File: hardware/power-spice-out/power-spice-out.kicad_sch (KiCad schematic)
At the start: 10 parts, among them Q1 Si7149ADP, Q2 NMOS, Q3 Si7149ADP

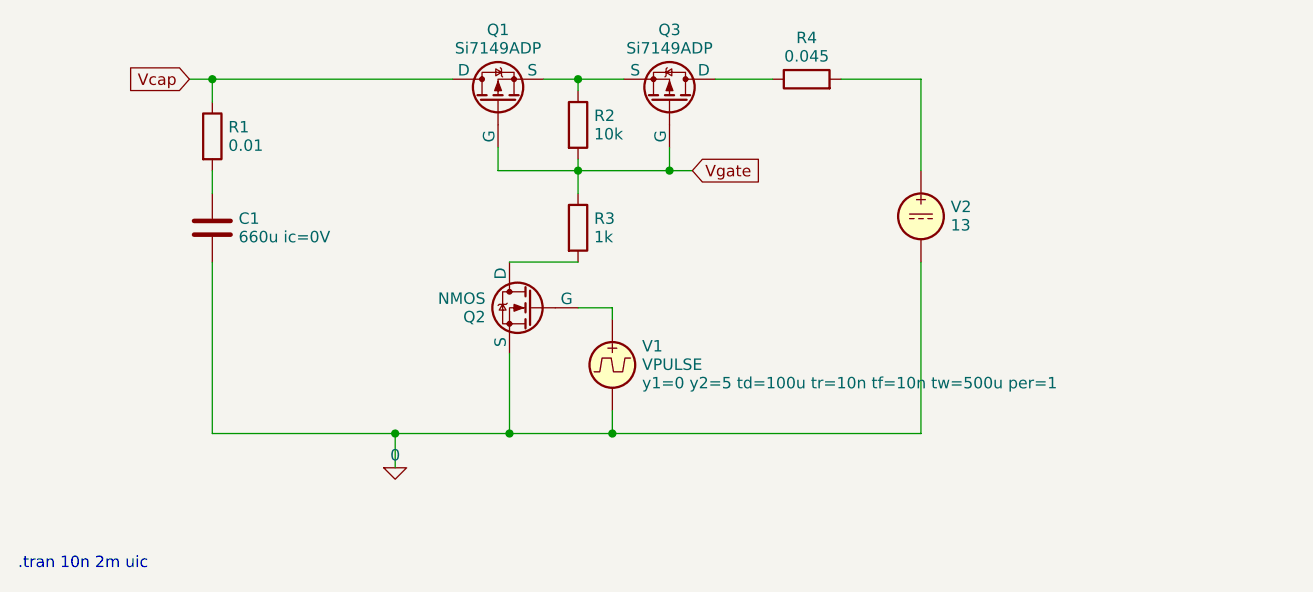
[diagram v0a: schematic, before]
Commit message: More accurate simulation with a BSS123 model and the 10k resistance from the control circuit. Doesn't change the peak transient current ...
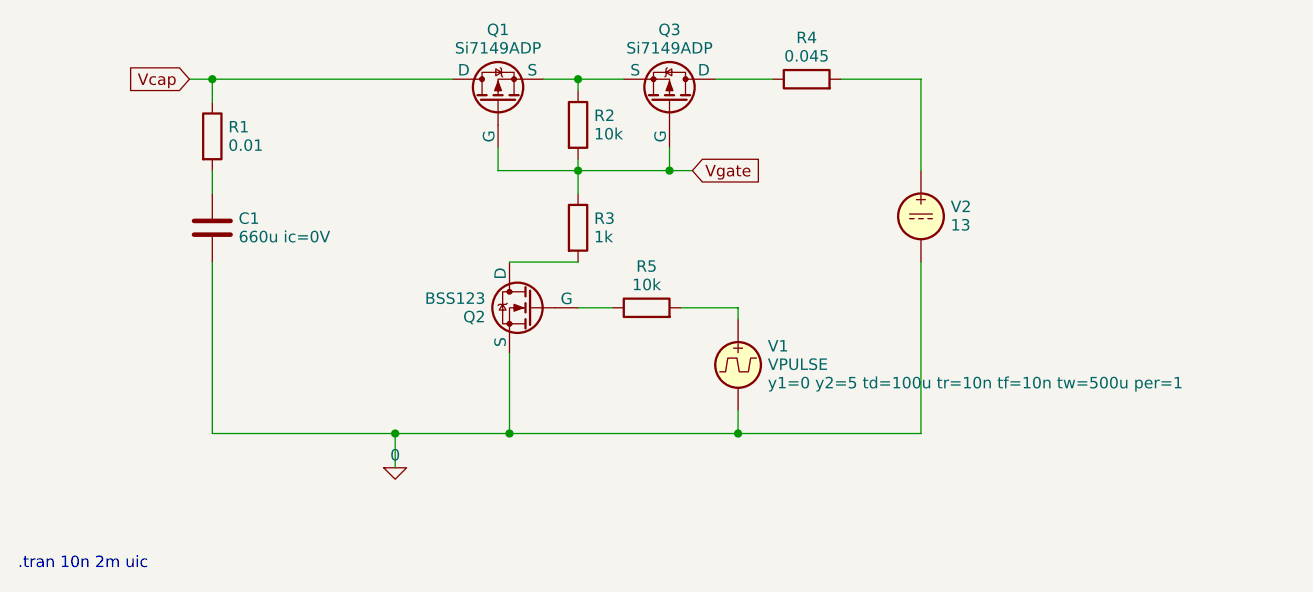
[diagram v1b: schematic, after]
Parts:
- added R5: 10k, symbol Device:R
- Q2: value NMOS -> BSS123
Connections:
- net at Q2.2 (G): now also R5.1; no longer V1.1
- new net: R5.2, V1.1
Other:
- moved on the sheet: V1
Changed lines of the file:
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@@
   (junction (at 116.84 91.44) (diameter 0) (color 0 0 0 0)
   )
-  (junction (at 161.29 130.81) (diameter 0) (color 0 0 0 0)
-  )
   (junction (at 149.86 130.81) (diameter 0) (color 0 0 0 0)
   )
   (junction (at 157.48 101.6) (diameter 0) (color 0 0 0 0)
   )
+  (junction (at 175.26 130.81) (diameter 0) (color 0 0 0 0)
+  )
   (junction (at 137.16 130.81) (diameter 0) (color 0 0 0 0)
   )
@@
     (stroke (width 0) (type default))
   )
-  (wire (pts (xy 161.29 130.81) (xy 149.86 130.81))
-    (stroke (width 0) (type default))
-  )
   (wire (pts (xy 172.72 91.44) (xy 179.07 91.44))
     (stroke (width 0) (type default))
@@
     (stroke (width 0) (type default))
   )
+  (wire (pts (xy 168.91 116.84) (xy 175.26 116.84))
+    (stroke (width 0) (type default))
+  )
+  (wire (pts (xy 149.86 130.81) (xy 175.26 130.81))
+    (stroke (width 0) (type default))
+  )
   (wire (pts (xy 149.86 130.81) (xy 137.16 130.81))
     (stroke (width 0) (type default))
@@
     (stroke (width 0) (type default))
   )
-  (wire (pts (xy 195.58 130.81) (xy 161.29 130.81))
+  (wire (pts (xy 195.58 130.81) (xy 175.26 130.81))
     (stroke (width 0) (type default))
   )
@@
     (stroke (width 0) (type default))
   )
-  (wire (pts (xy 161.29 128.27) (xy 161.29 130.81))
+  (wire (pts (xy 175.26 128.27) (xy 175.26 130.81))
     (stroke (width 0) (type default))
   )
@@
     (stroke (width 0) (type default))
   )
-  (wire (pts (xy 161.29 116.84) (xy 161.29 118.11))
+  (wire (pts (xy 175.26 116.84) (xy 175.26 118.11))
     (stroke (width 0) (type default))
   )
@@
     )
   )
+  (symbol (lib_id "Device:R") (at 165.1 116.84 90) (unit 1)
+    (in_bom yes) (on_board yes) (dnp no) (fields_autoplaced)
+    (property "Reference" "R5" (at 165.1 112.244 90)
+      (effects (font (size 1.27 1.27)))
+    )
+    (property "Value" "10k" (at 165.1 114.292 90)
+      (effects (font (size 1.27 1.27)))
+    )
+    (property "Footprint" "" (at 165.1 118.618 90)
+      (effects (font (size 1.27 1.27)) hide)
+    )
+    (property "Datasheet" "~" (at 165.1 116.84 0)
+      (effects (font (size 1.27 1.27)) hide)
+    )
+    (property "P/N" "" (at 165.1 116.84 0)
+      (effects (font (size 1.27 1.27)) hide)
+    )
+    (pin "1")
+    (pin "2")
+    (instances
+      (project "power-spice-out"
+        (path "/3b519c6d-240e-4784-9341-b4b14767d2f5"
+          (reference "R5") (unit 1)
+        )
+      )
+    )
+  )
   (symbol (lib_id "Simulation_SPICE:NMOS") (at 152.4 116.84 0) (mirror y) (unit 1)
     (in_bom yes) (on_board yes) (dnp no)
@@
       (effects (font (size 1.27 1.27)) (justify left))
     )
-    (property "Value" "NMOS" (at 147.1931 115.816 0)
+    (property "Value" "BSS123" (at 147.1931 115.816 0)
       (effects (font (size 1.27 1.27)) (justify left))
     )
@@
       (effects (font (size 1.27 1.27)) hide)
     )
-    (property "Sim.Device" "NMOS" (at 152.4 133.985 0)
-      (effects (font (size 1.27 1.27)) hide)
-    )
-    (property "Sim.Type" "VDMOS" (at 152.4 135.89 0)
-      (effects (font (size 1.27 1.27)) hide)
-    )
-    (property "Sim.Pins" "1=D 2=G 3=S" (at 152.4 132.08 0)
+    (property "Sim.Device" "SUBCKT" (at 152.4 133.985 0)
+      (effects (font (size 1.27 1.27)) hide)
+    )
+    (property "Sim.Pins" "1=3 2=4 3=5" (at 152.4 132.08 0)
       (effects (font (size 1.27 1.27)) hide)
     )
@@
       (effects (font (size 1.27 1.27)) hide)
     )
+    (property "Sim.Library" "BSS123.LIB" (at 152.4 116.84 0)
+      (effects (font (size 1.27 1.27)) hide)
+    )
+    (property "Sim.Name" "BSS123/ZTX" (at 152.4 116.84 0)
+      (effects (font (size 1.27 1.27)) hide)
+    )
     (pin "1")
     (pin "2")
@@
     )
   )
-  (symbol (lib_id "Simulation_SPICE:VPULSE") (at 161.29 123.19 0) (unit 1)
-    (in_bom yes) (on_board yes) (dnp no) (fields_autoplaced)
-    (property "Reference" "V1" (at 164.592 121.1062 0)
-      (effects (font (size 1.27 1.27)) (justify left))
-    )
-    (property "Value" "VPULSE" (at 164.592 123.1542 0)
-      (effects (font (size 1.27 1.27)) (justify left))
-    )
-    (property "Footprint" "" (at 161.29 123.19 0)
-      (effects (font (size 1.27 1.27)) hide)
-    )
-    (property "Datasheet" "~" (at 161.29 123.19 0)
-      (effects (font (size 1.27 1.27)) hide)
-    )
-    (property "Sim.Pins" "1=+ 2=-" (at 161.29 123.19 0)
-      (effects (font (size 1.27 1.27)) hide)
-    )
-    (property "Sim.Type" "PULSE" (at 161.29 123.19 0)
-      (effects (font (size 1.27 1.27)) hide)
-    )
-    (property "Sim.Device" "V" (at 161.29 123.19 0)
+  (symbol (lib_id "Simulation_SPICE:VPULSE") (at 175.26 123.19 0) (unit 1)
+    (in_bom yes) (on_board yes) (dnp no) (fields_autoplaced)
+    (property "Reference" "V1" (at 178.562 121.1062 0)
+      (effects (font (size 1.27 1.27)) (justify left))
+    )
+    (property "Value" "VPULSE" (at 178.562 123.1542 0)
+      (effects (font (size 1.27 1.27)) (justify left))
+    )
+    (property "Footprint" "" (at 175.26 123.19 0)
+      (effects (font (size 1.27 1.27)) hide)
+    )
+    (property "Datasheet" "~" (at 175.26 123.19 0)
+      (effects (font (size 1.27 1.27)) hide)
+    )
+    (property "Sim.Pins" "1=+ 2=-" (at 175.26 123.19 0)
+      (effects (font (size 1.27 1.27)) hide)
+    )
+    (property "Sim.Type" "PULSE" (at 175.26 123.19 0)
+      (effects (font (size 1.27 1.27)) hide)
+    )
+    (property "Sim.Device" "V" (at 175.26 123.19 0)
       (effects (font (size 1.27 1.27)) (justify left) hide)
     )
-    (property "Sim.Params" "y1=0 y2=5 td=100u tr=10n tf=10n tw=500u per=1" (at 164.592 125.2022 0)
-      (effects (font (size 1.27 1.27)) (justify left))
-    )
+    (property "Sim.Params" "y1=0 y2=5 td=100u tr=10n tf=10n tw=500u per=1" (at 178.562 125.2022 0)
+      (effects (font (size 1.27 1.27)) (justify left))
+    )

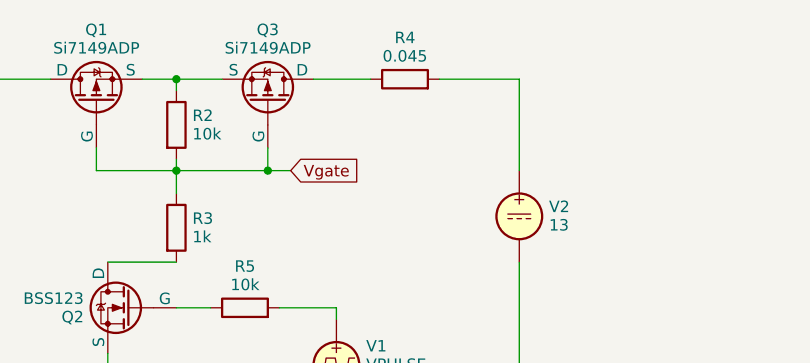
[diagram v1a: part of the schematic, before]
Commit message: Correct "shunt+cables" resistor value (shunt is 2mO, not 20mO)
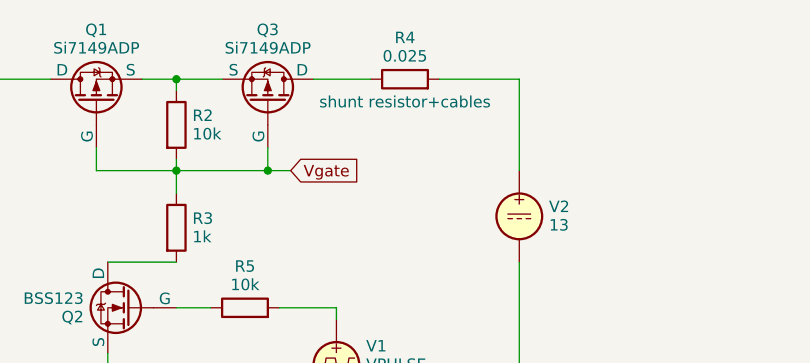
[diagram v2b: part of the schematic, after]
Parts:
- R4: value 0.045 -> 0.025; comment (none) -> shunt resistor+cables
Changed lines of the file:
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@@
   )
   (symbol (lib_id "Device:R") (at 182.88 91.44 90) (unit 1)
-    (in_bom yes) (on_board yes) (dnp no) (fields_autoplaced)
+    (in_bom yes) (on_board yes) (dnp no)
     (property "Reference" "R4" (at 182.88 86.844 90)
       (effects (font (size 1.27 1.27)))
     )
-    (property "Value" "0.045" (at 182.88 88.892 90)
+    (property "Value" "0.025" (at 182.88 88.892 90)
       (effects (font (size 1.27 1.27)))
     )
@@
       (effects (font (size 1.27 1.27)) hide)
     )
+    (property "comment" "shunt resistor+cables" (at 182.88 93.98 90)
+      (effects (font (size 1.27 1.27)))
+    )
     (pin "1")

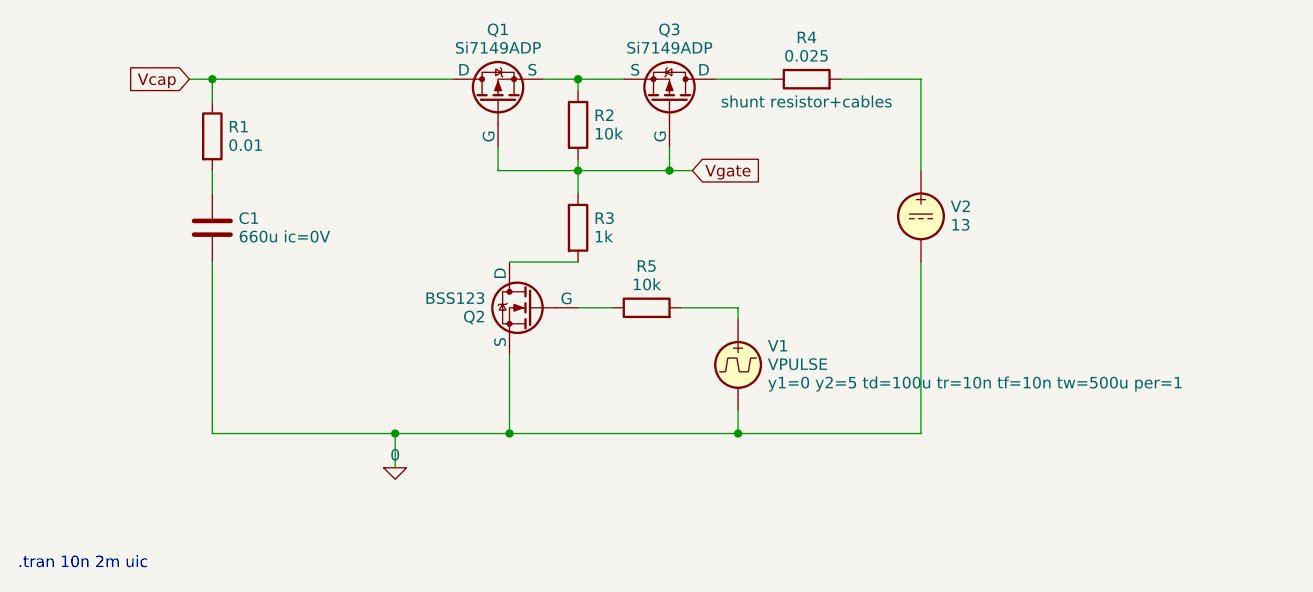
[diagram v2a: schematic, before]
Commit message: Bump R3 from 1k to 4.7k. This décreases the inrush current from about 200A to 130. The Vgs is decreased by about 3V (from 12 to 9) which shouldn't affect much the Rsdon of the Si7149.
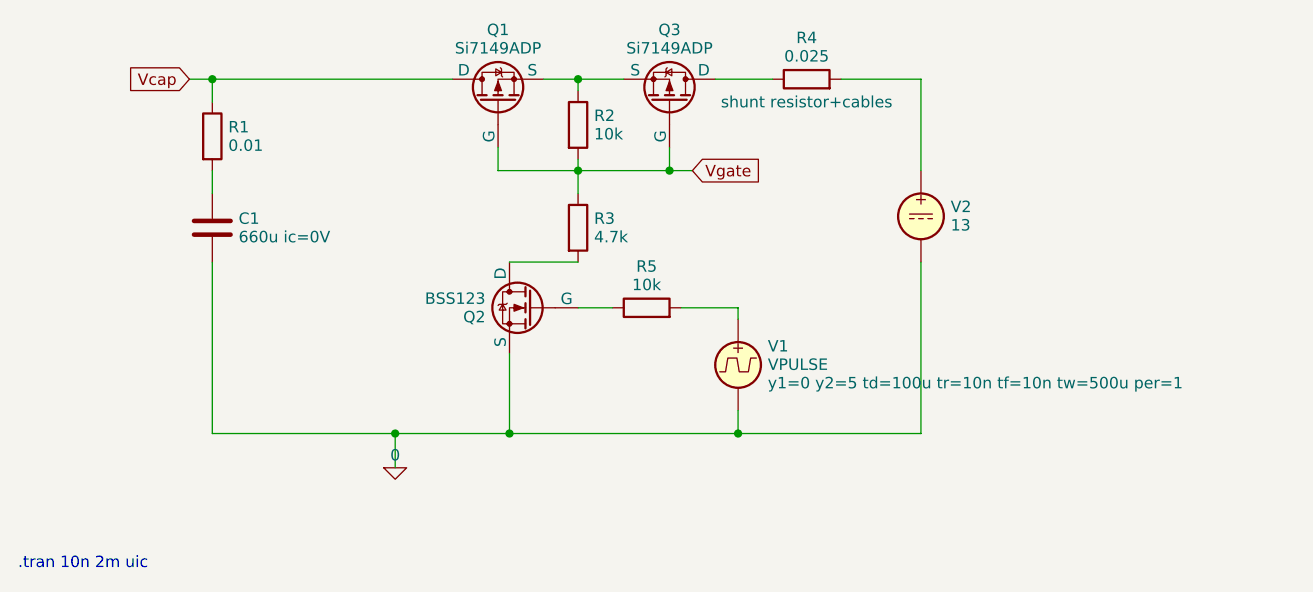
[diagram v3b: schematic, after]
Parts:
- R3: value 1k -> 4.7k
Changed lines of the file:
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@@
       (effects (font (size 1.27 1.27)) (justify left))
     )
-    (property "Value" "1k" (at 159.258 108.974 0)
+    (property "Value" "4.7k" (at 159.258 108.974 0)
       (effects (font (size 1.27 1.27)) (justify left))
     )
